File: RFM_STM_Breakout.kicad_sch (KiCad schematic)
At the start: 29 parts, among them J1 USB_B_Micro, J2 Conn_01x02_Male, J3 Conn_01x16_Male, J4 Conn_01x12_Male, J5 Conn_01x15_Male, J6 Conn_Coaxial, SW1 SW_Push, U1 RFM95W-868S2, U2 XC6206P332MR, U3 STM32L053R8Tx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

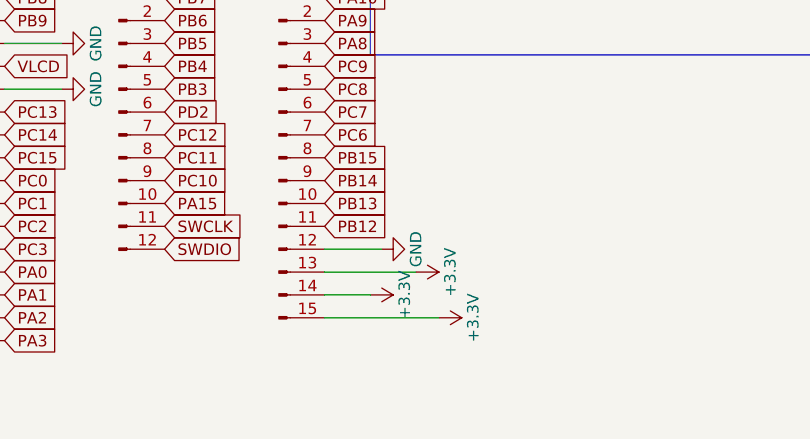
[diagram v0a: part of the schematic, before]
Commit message: Change angles and 3.3V Rail
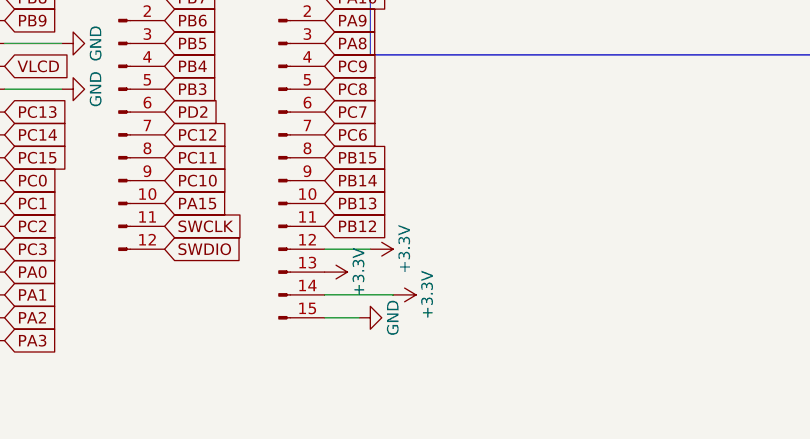
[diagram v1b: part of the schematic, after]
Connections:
- net +3.3V: now also J5.12 (Pin_12); no longer J5.15 (Pin_15)
- net GND: now also J5.15 (Pin_15); no longer J5.12 (Pin_12)
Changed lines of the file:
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@@
-    (stroke (width 0) (type default) (color 0 0 0 0))
-  )
-  (wire (pts (xy 153.67 182.88) (xy 166.37 182.88))
-    (stroke (width 0) (type default) (color 0 0 0 0))
-  )
-  (wire (pts (xy 153.67 177.8) (xy 163.83 177.8))
     (stroke (width 0) (type default) (color 0 0 0 0))
   )
@@
     (stroke (width 0) (type default) (color 0 0 0 0))
   )
-  (wire (pts (xy 153.67 180.34) (xy 158.75 180.34))
-    (stroke (width 0) (type default) (color 0 0 0 0))
-  )
   (wire (pts (xy 41.91 69.85) (xy 31.75 69.85))
     (stroke (width 0) (type default) (color 0 0 0 0))
@@
     (stroke (width 0) (type default) (color 0 0 0 0))
   )
+  (wire (pts (xy 153.67 182.88) (xy 157.48 182.88))
+    (stroke (width 0) (type default) (color 0 0 0 0))
+  )
   (wire (pts (xy 231.14 137.16) (xy 233.68 137.16))
     (stroke (width 0) (type default) (color 0 0 0 0))
@@
     (stroke (width 0) (type default) (color 0 0 0 0))
   )
+  (wire (pts (xy 153.67 180.34) (xy 161.29 180.34))
+    (stroke (width 0) (type default) (color 0 0 0 0))
+  )
   (wire (pts (xy 31.75 77.47) (xy 31.75 76.2))
     (stroke (width 0) (type default) (color 0 0 0 0))
@@
     (stroke (width 0) (type default) (color 0 0 0 0))
   )
-  (wire (pts (xy 153.67 175.26) (xy 160.02 175.26))
-    (stroke (width 0) (type default) (color 0 0 0 0))
-  )
   (wire (pts (xy 21.59 95.25) (xy 21.59 96.52))
     (stroke (width 0) (type default) (color 0 0 0 0))
@@
   )
   (wire (pts (xy 52.07 71.12) (xy 52.07 69.85))
+    (stroke (width 0) (type default) (color 0 0 0 0))
+  )
+  (wire (pts (xy 153.67 175.26) (xy 158.75 175.26))
     (stroke (width 0) (type default) (color 0 0 0 0))
   )
@@
     (pin "1")
   )
+  (symbol (lib_id "power:+3.3V") (at 153.67 177.8 270) (unit 1)
+    (in_bom yes) (on_board yes)
+    (property "Reference" "#PWR0126" (id 0) (at 149.86 177.8 0)
+      (effects (font (size 1.27 1.27)) hide)
+    )
+    (property "Value" "+3.3V" (id 1) (at 157.48 177.8 0))
+    (property "Footprint" "" (id 2) (at 153.67 177.8 0)
+      (effects (font (size 1.27 1.27)) hide)
+    )
+    (property "Datasheet" "" (id 3) (at 153.67 177.8 0)
+      (effects (font (size 1.27 1.27)) hide)
+    )
+    (pin "1")
+  )
+  (symbol (lib_id "power:GND") (at 157.48 182.88 90) (unit 1)
+    (in_bom yes) (on_board yes)
+    (property "Reference" "#PWR0129" (id 0) (at 163.83 182.88 0)
+      (effects (font (size 1.27 1.27)) hide)
+    )
+    (property "Value" "GND" (id 1) (at 161.29 182.88 0))
+    (property "Footprint" "" (id 2) (at 157.48 182.88 0)
+      (effects (font (size 1.27 1.27)) hide)
+    )
+    (property "Datasheet" "" (id 3) (at 157.48 182.88 0)
+      (effects (font (size 1.27 1.27)) hide)
+    )
+    (pin "1")
+  )
   (symbol (lib_id "power:+3.3V") (at 266.7 71.12 0) (unit 1)
     (in_bom yes) (on_board yes)
@@
     (pin "1")
   )
+  (symbol (lib_id "power:+3.3V") (at 158.75 175.26 270) (unit 1)
+    (in_bom yes) (on_board yes)
+    (property "Reference" "#PWR0127" (id 0) (at 154.94 175.26 0)
+      (effects (font (size 1.27 1.27)) hide)
+    )
+    (property "Value" "+3.3V" (id 1) (at 162.56 175.26 0))
+    (property "Footprint" "" (id 2) (at 158.75 175.26 0)
+      (effects (font (size 1.27 1.27)) hide)
+    )
+    (property "Datasheet" "" (id 3) (at 158.75 175.26 0)
+      (effects (font (size 1.27 1.27)) hide)
+    )
+    (pin "1")
+  )
   (symbol (lib_id "power:+3.3V") (at 81.28 26.67 0) (unit 1)
     (in_bom yes) (on_board yes)
@@
     )
     (property "Datasheet" "" (id 3) (at 81.28 26.67 0)
-      (effects (font (size 1.27 1.27)) hide)
-    )
-    (pin "1")
-  )
-  (symbol (lib_id "power:+3.3V") (at 166.37 182.88 270) (unit 1)
-    (in_bom yes) (on_board yes)
-    (property "Reference" "#PWR?" (id 0) (at 162.56 182.88 0)
-      (effects (font (size 1.27 1.27)) hide)
-    )
-    (property "Value" "+3.3V" (id 1) (at 170.18 182.88 0))
-    (property "Footprint" "" (id 2) (at 166.37 182.88 0)
-      (effects (font (size 1.27 1.27)) hide)
-    )
-    (property "Datasheet" "" (id 3) (at 166.37 182.88 0)
-      (effects (font (size 1.27 1.27)) hide)
-    )
-    (pin "1")
-  )
-  (symbol (lib_id "power:GND") (at 160.02 175.26 90) (unit 1)
-    (in_bom yes) (on_board yes)
-    (property "Reference" "#PWR?" (id 0) (at 166.37 175.26 0)
-      (effects (font (size 1.27 1.27)) hide)
-    )
-    (property "Value" "GND" (id 1) (at 163.83 175.26 0))
-    (property "Footprint" "" (id 2) (at 160.02 175.26 0)
-      (effects (font (size 1.27 1.27)) hide)
-    )
-    (property "Datasheet" "" (id 3) (at 160.02 175.26 0)
       (effects (font (size 1.27 1.27)) hide)
     )
@@
     (pin "1")
     (pin "2")
-  )
-  (symbol (lib_id "power:+3.3V") (at 163.83 177.8 270) (unit 1)
-    (in_bom yes) (on_board yes)
-    (property "Reference" "#PWR?" (id 0) (at 160.02 177.8 0)
-      (effects (font (size 1.27 1.27)) hide)
-    )
-    (property "Value" "+3.3V" (id 1) (at 167.64 177.8 0))
-    (property "Footprint" "" (id 2) (at 163.83 177.8 0)
-      (effects (font (size 1.27 1.27)) hide)
-    )
-    (property "Datasheet" "" (id 3) (at 163.83 177.8 0)
-      (effects (font (size 1.27 1.27)) hide)
-    )
-    (pin "1")
   )
   (symbol (lib_id "MCU_ST_STM32L0:STM32L053R8Tx") (at 236.22 91.44 0) (unit 1)
@@
     (pin "2")
   )
+  (symbol (lib_id "power:+3.3V") (at 161.29 180.34 270) (unit 1)
+    (in_bom yes) (on_board yes)
+    (property "Reference" "#PWR0128" (id 0) (at 157.48 180.34 0)
+      (effects (font (size 1.27 1.27)) hide)
+    )
+    (property "Value" "+3.3V" (id 1) (at 165.1 180.34 0))
+    (property "Footprint" "" (id 2) (at 161.29 180.34 0)
+      (effects (font (size 1.27 1.27)) hide)
+    )
+    (property "Datasheet" "" (id 3) (at 161.29 180.34 0)
+      (effects (font (size 1.27 1.27)) hide)
+    )
+    (pin "1")
+  )
   (symbol (lib_id "RF_Module:RFM95W-868S2") (at 63.5 158.75 0) (unit 1)
     (in_bom yes) (on_board yes) (fields_autoplaced)
@@
     (pin "1")
   )
-  (symbol (lib_id "power:+3.3V") (at 158.75 180.34 270) (unit 1)
-    (in_bom yes) (on_board yes)
-    (property "Reference" "#PWR?" (id 0) (at 154.94 180.34 0)
-      (effects (font (size 1.27 1.27)) hide)
-    )
-    (property "Value" "+3.3V" (id 1) (at 162.56 180.34 0))
-    (property "Footprint" "" (id 2) (at 158.75 180.34 0)
-      (effects (font (size 1.27 1.27)) hide)
-    )
-    (property "Datasheet" "" (id 3) (at 158.75 180.34 0)
-      (effects (font (size 1.27 1.27)) hide)
-    )
-    (pin "1")
-  )
   (symbol (lib_id "Device:C_Small") (at 43.18 100.33 0) (unit 1)
     (in_bom yes) (on_board yes)
@@
       (reference "#PWR0125") (unit 1) (value "GND") (footprint "")
     )
+    (path "/087aa7b6-f0d9-402a-b265-21bd56d74f31"
+      (reference "#PWR0126") (unit 1) (value "+3.3V") (footprint "")
+    )
+    (path "/4209145a-70b5-44e7-88b4-8f19c64986a9"
+      (reference "#PWR0127") (unit 1) (value "+3.3V") (footprint "")
+    )
+    (path "/ac6c6756-3d0a-43c1-a57b-35b911279651"
+      (reference "#PWR0128") (unit 1) (value "+3.3V") (footprint "")
+    )
+    (path "/1537212c-8d17-45c0-83e8-ad8f5f8b976a"
+      (reference "#PWR0129") (unit 1) (value "GND") (footprint "")
+    )
     (path "/97c89f45-da59-40ef-a170-91146e846dc4"
       (reference "#PWR0130") (unit 1) (value "GND") (footprint "")
@@
       (reference "#PWR0131") (unit 1) (value "GND") (footprint "")
     )
-    (path "/43ef5c91-9545-465e-a592-472bf3f74ee2"
-      (reference "#PWR?") (unit 1) (value "+3.3V") (footprint "")
-    )
-    (path "/4ad02204-a3ba-462e-a0dc-b15d074f6a4b"
-      (reference "#PWR?") (unit 1) (value "GND") (footprint "")
-    )
-    (path "/a5c89935-32cd-4dab-9cec-f9b3ce756ff1"
-      (reference "#PWR?") (unit 1) (value "+3.3V") (footprint "")
-    )
-    (path "/df452ea3-1461-4993-86c1-81c12306da23"
-      (reference "#PWR?") (unit 1) (value "+3.3V") (footprint "")
-    )
     (path "/769e8e23-d256-42d8-88dd-29a898017a0d"
